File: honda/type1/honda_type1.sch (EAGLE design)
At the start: 3 parts, among them J1 501645-2620, J2 501645-3620

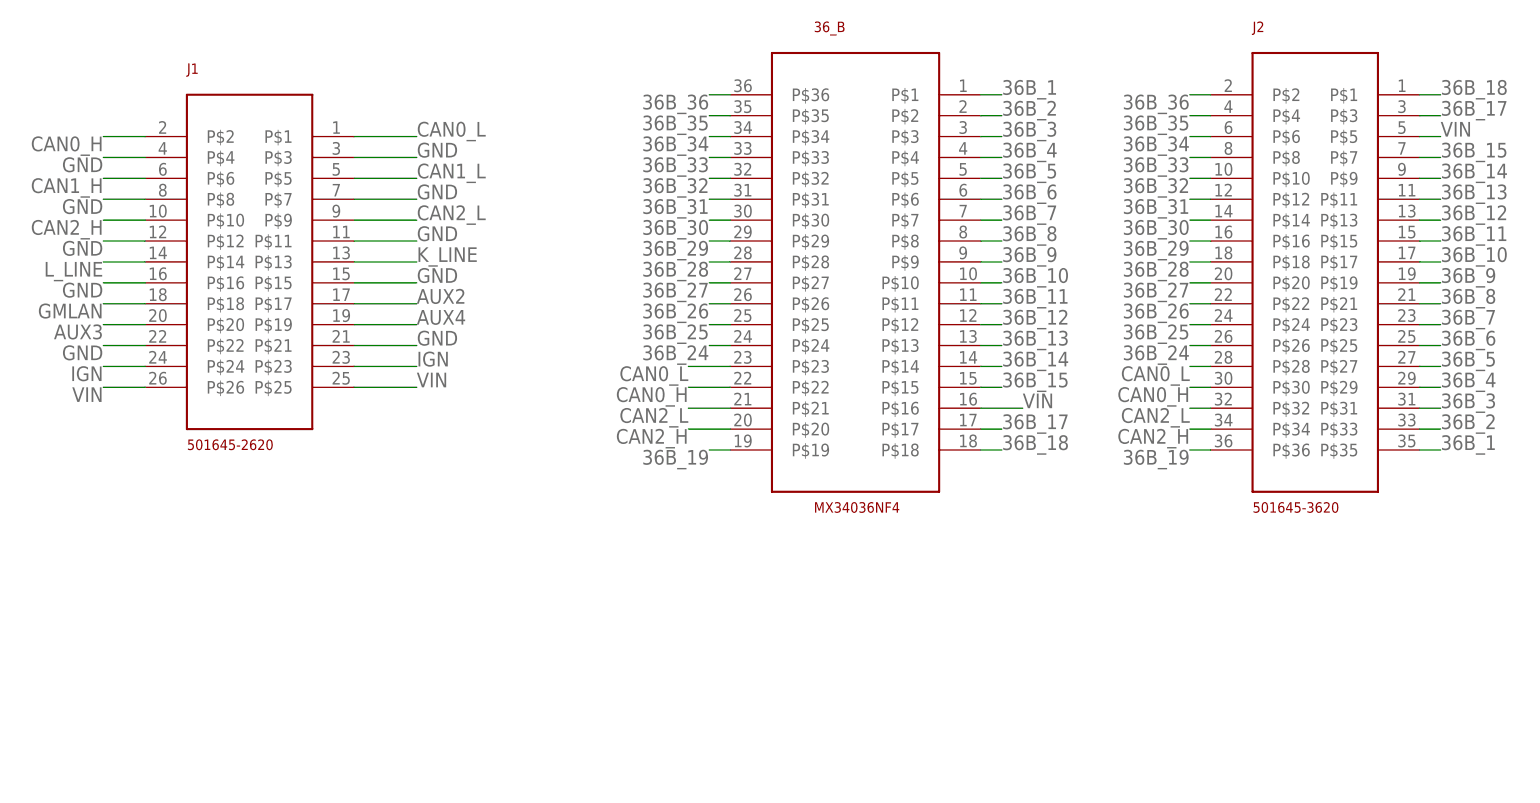
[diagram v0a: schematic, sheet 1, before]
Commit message: switch to rj45 for the interconnect
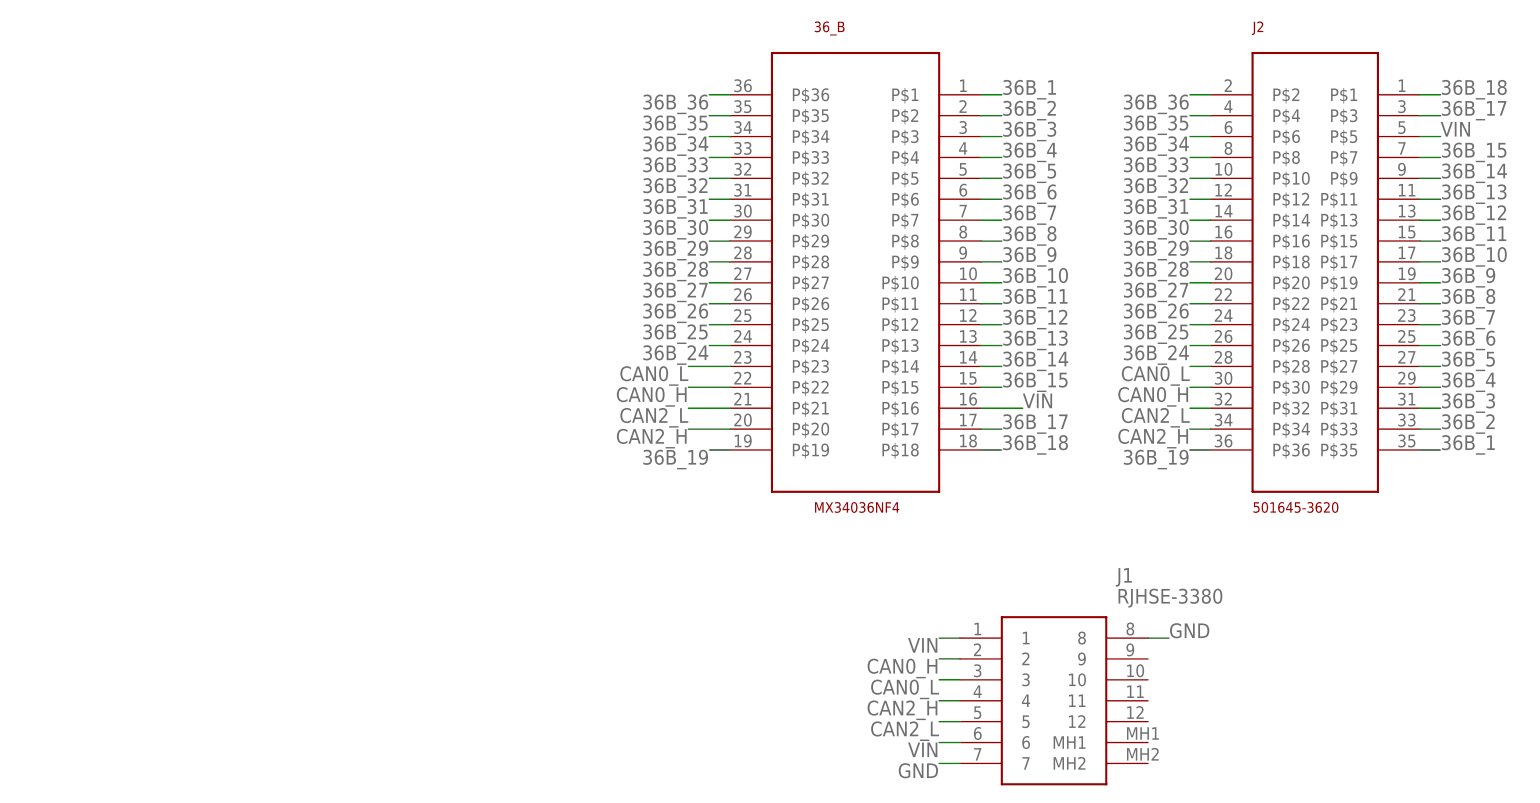
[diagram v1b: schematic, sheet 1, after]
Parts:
- J1: value 501645-2620 -> RJHSE-3380; device Souers:501645-2620 -> RJHSE-3380:RJHSE-3380
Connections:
- removed net AUX2: J1.P$17
- removed net AUX3: J1.P$20
- removed net AUX4: J1.P$19
- removed net CAN1_H: J1.P$6
- removed net CAN1_L: J1.P$5
- removed net GMLAN: J1.P$18
- removed net IGN: J1.P$23, J1.P$24
- removed net K_LINE: J1.P$13
- removed net L_LINE: J1.P$14
- net CAN0_H: now also J1.2; no longer J1.P$2
- net CAN0_L: now also J1.3; no longer J1.P$1
- net CAN2_H: now also J1.4; no longer J1.P$10
- net CAN2_L: now also J1.5; no longer J1.P$9
- net GND: now also J1.7, J1.8; no longer J1.P$11, J1.P$12, J1.P$15, J1.P$16, J1.P$21, J1.P$22, J1.P$3, J1.P$4, J1.P$7, J1.P$8
- net VIN: now also J1.1, J1.6; no longer J1.P$25, J1.P$26
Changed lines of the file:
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@@
 <parts>
 <part name="36_B" library="Souers" deviceset="MX34036NF4" device=""/>
-<part name="J1" library="Souers" deviceset="501645-2620" device=""/>
 <part name="J2" library="Souers" deviceset="501645-3620" device=""/>
+<part name="J1" library="RJHSE-3380" deviceset="RJHSE-3380" device=""/>
 </parts>
 <sheets>
@@
 <instances>
 <instance part="36_B" gate="G$1" x="22.86" y="10.16"/>
-<instance part="J1" gate="G$1" x="-58.42" y="7.62"/>
 <instance part="J2" gate="G$1" x="71.12" y="12.7"/>
+<instance part="J1" gate="G$1" x="33.02" y="-35.56"/>
 </instances>
 <busses>
 </busses>
 <nets>
-<net name="GND" class="0">
-<segment>
-<pinref part="J1" gate="G$1" pin="P$3"/>
-<wire x1="-40.64" y1="22.86" x2="-33.02" y2="22.86" width="0.1524" layer="91"/>
-<label x="-33.02" y="22.86" size="1.778" layer="95"/>
-</segment>
-<segment>
-<pinref part="J1" gate="G$1" pin="P$4"/>
-<wire x1="-66.04" y1="22.86" x2="-71.12" y2="22.86" width="0.1524" layer="91"/>
-<label x="-71.12" y="22.86" size="1.778" layer="95" rot="R180"/>
-</segment>
-<segment>
-<pinref part="J1" gate="G$1" pin="P$8"/>
-<wire x1="-66.04" y1="17.78" x2="-71.12" y2="17.78" width="0.1524" layer="91"/>
-<label x="-71.12" y="17.78" size="1.778" layer="95" rot="R180"/>
-</segment>
-<segment>
-<pinref part="J1" gate="G$1" pin="P$7"/>
-<wire x1="-40.64" y1="17.78" x2="-33.02" y2="17.78" width="0.1524" layer="91"/>
-<label x="-33.02" y="17.78" size="1.778" layer="95"/>
-</segment>
-<segment>
-<pinref part="J1" gate="G$1" pin="P$11"/>
-<wire x1="-40.64" y1="12.7" x2="-33.02" y2="12.7" width="0.1524" layer="91"/>
-<label x="-33.02" y="12.7" size="1.778" layer="95"/>
-</segment>
-<segment>
-<pinref part="J1" gate="G$1" pin="P$12"/>
-<wire x1="-66.04" y1="12.7" x2="-71.12" y2="12.7" width="0.1524" layer="91"/>
-<label x="-71.12" y="12.7" size="1.778" layer="95" rot="R180"/>
-</segment>
-<segment>
-<pinref part="J1" gate="G$1" pin="P$21"/>
-<wire x1="-40.64" y1="0" x2="-33.02" y2="0" width="0.1524" layer="91"/>
-<label x="-33.02" y="0" size="1.778" layer="95"/>
-</segment>
-<segment>
-<pinref part="J1" gate="G$1" pin="P$22"/>
-<wire x1="-66.04" y1="0" x2="-71.12" y2="0" width="0.1524" layer="91"/>
-<label x="-71.12" y="0" size="1.778" layer="95" rot="R180"/>
-</segment>
-<segment>
-<pinref part="J1" gate="G$1" pin="P$16"/>
-<wire x1="-66.04" y1="7.62" x2="-71.12" y2="7.62" width="0.1524" layer="91"/>
-<label x="-71.12" y="7.62" size="1.778" layer="95" rot="R180"/>
-</segment>
-<segment>
-<pinref part="J1" gate="G$1" pin="P$15"/>
-<wire x1="-40.64" y1="7.62" x2="-33.02" y2="7.62" width="0.1524" layer="91"/>
-<label x="-33.02" y="7.62" size="1.778" layer="95"/>
-</segment>
-</net>
-<net name="K_LINE" class="0">
-<segment>
-<pinref part="J1" gate="G$1" pin="P$13"/>
-<wire x1="-40.64" y1="10.16" x2="-33.02" y2="10.16" width="0.1524" layer="91"/>
-<label x="-33.02" y="10.16" size="1.778" layer="95"/>
-</segment>
-</net>
 <net name="VIN" class="1">
 <segment>
@@
 </segment>
 <segment>
-<pinref part="J1" gate="G$1" pin="P$25"/>
-<wire x1="-40.64" y1="-5.08" x2="-33.02" y2="-5.08" width="0.1524" layer="91"/>
-<label x="-33.02" y="-5.08" size="1.778" layer="95"/>
-</segment>
-<segment>
-<pinref part="J1" gate="G$1" pin="P$26"/>
-<wire x1="-66.04" y1="-5.08" x2="-71.12" y2="-5.08" width="0.1524" layer="91"/>
-<label x="-71.12" y="-5.08" size="1.778" layer="95" rot="R180"/>
-</segment>
-<segment>
 <pinref part="J2" gate="G$1" pin="P$5"/>
 <wire x1="88.9" y1="25.4" x2="91.44" y2="25.4" width="0.1524" layer="91"/>
 <label x="91.44" y="25.4" size="1.778" layer="95"/>
 </segment>
+<segment>
+<pinref part="J1" gate="G$1" pin="1"/>
+<wire x1="33.02" y1="-35.56" x2="30.48" y2="-35.56" width="0.1524" layer="91"/>
+<label x="30.48" y="-35.56" size="1.778" layer="95" rot="R180"/>
+</segment>
+<segment>
+<pinref part="J1" gate="G$1" pin="6"/>
+<wire x1="33.02" y1="-48.26" x2="30.48" y2="-48.26" width="0.1524" layer="91"/>
+<label x="30.48" y="-48.26" size="1.778" layer="95" rot="R180"/>
+</segment>
 </net>
 <net name="CAN2_H" class="0">
@@
 </segment>
 <segment>
-<pinref part="J1" gate="G$1" pin="P$10"/>
-<wire x1="-66.04" y1="15.24" x2="-71.12" y2="15.24" width="0.1524" layer="91"/>
-<label x="-71.12" y="15.24" size="1.778" layer="95" rot="R180"/>
-</segment>
-<segment>
 <pinref part="J2" gate="G$1" pin="P$34"/>
 <wire x1="63.5" y1="-10.16" x2="60.96" y2="-10.16" width="0.1524" layer="91"/>
 <label x="60.96" y="-10.16" size="1.778" layer="95" rot="R180"/>
 </segment>
+<segment>
+<pinref part="J1" gate="G$1" pin="4"/>
+<wire x1="33.02" y1="-43.18" x2="30.48" y2="-43.18" width="0.1524" layer="91"/>
+<label x="30.48" y="-43.18" size="1.778" layer="95" rot="R180"/>
+</segment>
 </net>
 <net name="CAN2_L" class="0">
@@
 </segment>
 <segment>
-<pinref part="J1" gate="G$1" pin="P$9"/>
-<wire x1="-40.64" y1="15.24" x2="-33.02" y2="15.24" width="0.1524" layer="91"/>
-<label x="-33.02" y="15.24" size="1.778" layer="95"/>
-</segment>
-<segment>
 <pinref part="J2" gate="G$1" pin="P$32"/>
 <wire x1="63.5" y1="-7.62" x2="60.96" y2="-7.62" width="0.1524" layer="91"/>
 <label x="60.96" y="-7.62" size="1.778" layer="95" rot="R180"/>
 </segment>
+<segment>
+<pinref part="J1" gate="G$1" pin="5"/>
+<wire x1="33.02" y1="-45.72" x2="30.48" y2="-45.72" width="0.1524" layer="91"/>
+<label x="30.48" y="-45.72" size="1.778" layer="95" rot="R180"/>
+</segment>
 </net>
 <net name="CAN0_H" class="0">
@@
 </segment>
 <segment>
-<pinref part="J1" gate="G$1" pin="P$2"/>
-<wire x1="-66.04" y1="25.4" x2="-71.12" y2="25.4" width="0.1524" layer="91"/>
-<label x="-71.12" y="25.4" size="1.778" layer="95" rot="R180"/>
-</segment>
-<segment>
 <pinref part="J2" gate="G$1" pin="P$30"/>
 <wire x1="63.5" y1="-5.08" x2="60.96" y2="-5.08" width="0.1524" layer="91"/>
 <label x="60.96" y="-5.08" size="1.778" layer="95" rot="R180"/>
 </segment>
+<segment>
+<pinref part="J1" gate="G$1" pin="2"/>
+<wire x1="33.02" y1="-38.1" x2="30.48" y2="-38.1" width="0.1524" layer="91"/>
+<label x="30.48" y="-38.1" size="1.778" layer="95" rot="R180"/>
+</segment>
 </net>
 <net name="CAN0_L" class="0">
@@
 </segment>
 <segment>
-<pinref part="J1" gate="G$1" pin="P$1"/>
-<wire x1="-40.64" y1="25.4" x2="-33.02" y2="25.4" width="0.1524" layer="91"/>
-<label x="-33.02" y="25.4" size="1.778" layer="95"/>
-</segment>
-<segment>
 <pinref part="J2" gate="G$1" pin="P$28"/>
 <wire x1="63.5" y1="-2.54" x2="60.96" y2="-2.54" width="0.1524" layer="91"/>
 <label x="60.96" y="-2.54" size="1.778" layer="95" rot="R180"/>
 </segment>
-</net>
-<net name="L_LINE" class="0">
-<segment>
-<pinref part="J1" gate="G$1" pin="P$14"/>
-<wire x1="-66.04" y1="10.16" x2="-71.12" y2="10.16" width="0.1524" layer="91"/>
-<label x="-71.12" y="10.16" size="1.778" layer="95" rot="R180"/>
-</segment>
-</net>
-<net name="IGN" class="1">
-<segment>
-<pinref part="J1" gate="G$1" pin="P$23"/>
-<wire x1="-40.64" y1="-2.54" x2="-33.02" y2="-2.54" width="0.1524" layer="91"/>
-<label x="-33.02" y="-2.54" size="1.778" layer="95"/>
-</segment>
-<segment>
-<pinref part="J1" gate="G$1" pin="P$24"/>
-<wire x1="-66.04" y1="-2.54" x2="-71.12" y2="-2.54" width="0.1524" layer="91"/>
-<label x="-71.12" y="-2.54" size="1.778" layer="95" rot="R180"/>
-</segment>
-</net>
-<net name="CAN1_L" class="0">
-<segment>
-<pinref part="J1" gate="G$1" pin="P$5"/>
-<wire x1="-40.64" y1="20.32" x2="-33.02" y2="20.32" width="0.1524" layer="91"/>
-<label x="-33.02" y="20.32" size="1.778" layer="95"/>
-</segment>
-</net>
-<net name="CAN1_H" class="0">
-<segment>
-<pinref part="J1" gate="G$1" pin="P$6"/>
-<wire x1="-66.04" y1="20.32" x2="-71.12" y2="20.32" width="0.1524" layer="91"/>
-<label x="-71.12" y="20.32" size="1.778" layer="95" rot="R180"/>
-</segment>
-</net>
-<net name="AUX2" class="0">
-<segment>
-<pinref part="J1" gate="G$1" pin="P$17"/>
-<wire x1="-40.64" y1="5.08" x2="-33.02" y2="5.08" width="0.1524" layer="91"/>
-<label x="-33.02" y="5.08" size="1.778" layer="95"/>
-</segment>
-</net>
-<net name="AUX3" class="0">
-<segment>
-<pinref part="J1" gate="G$1" pin="P$20"/>
-<wire x1="-66.04" y1="2.54" x2="-71.12" y2="2.54" width="0.1524" layer="91"/>
-<label x="-71.12" y="2.54" size="1.778" layer="95" rot="R180"/>
-</segment>
-</net>
-<net name="AUX4" class="0">
-<segment>
-<pinref part="J1" gate="G$1" pin="P$19"/>
-<wire x1="-40.64" y1="2.54" x2="-33.02" y2="2.54" width="0.1524" layer="91"/>
-<label x="-33.02" y="2.54" size="1.778" layer="95"/>
-</segment>
-</net>
-<net name="GMLAN" class="0">
-<segment>
-<pinref part="J1" gate="G$1" pin="P$18"/>
-<wire x1="-66.04" y1="5.08" x2="-71.12" y2="5.08" width="0.1524" layer="91"/>
-<label x="-71.12" y="5.08" size="1.778" layer="95" rot="R180"/>
+<segment>
+<pinref part="J1" gate="G$1" pin="3"/>
+<wire x1="33.02" y1="-40.64" x2="30.48" y2="-40.64" width="0.1524" layer="91"/>
+<label x="30.48" y="-40.64" size="1.778" layer="95" rot="R180"/>
 </segment>
 </net>
@@
 </segment>
 </net>
+<net name="GND" class="1">
+<segment>
+<pinref part="J1" gate="G$1" pin="8"/>
+<wire x1="55.88" y1="-35.56" x2="58.42" y2="-35.56" width="0.1524" layer="91"/>
+<label x="58.42" y="-35.56" size="1.778" layer="95"/>
+</segment>
+<segment>
+<pinref part="J1" gate="G$1" pin="7"/>
+<wire x1="33.02" y1="-50.8" x2="30.48" y2="-50.8" width="0.1524" layer="91"/>
+<label x="30.48" y="-50.8" size="1.778" layer="95" rot="R180"/>
+</segment>
+</net>

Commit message: push
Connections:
- removed net CAN0_H: 36_B.P$22, J1.2, J2.P$30
- removed net CAN0_L: 36_B.P$23, J1.3, J2.P$28
- new net CAN1_H: 36_B.P$20, J1.4, J2.P$34
- new net CAN1_L: 36_B.P$21, J1.5, J2.P$32
- net CAN2_H: now also 36_B.P$22, J1.2, J2.P$30; no longer 36_B.P$20, J1.4, J2.P$34
- net CAN2_L: now also 36_B.P$23, J1.3, J2.P$28; no longer 36_B.P$21, J1.5, J2.P$32
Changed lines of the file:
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@@
 </segment>
 </net>
-<net name="CAN2_H" class="0">
+<net name="CAN1_H" class="0">
 <segment>
 <pinref part="36_B" gate="G$1" pin="P$20"/>
@@
 </segment>
 </net>
-<net name="CAN2_L" class="0">
+<net name="CAN1_L" class="0">
 <segment>
 <pinref part="36_B" gate="G$1" pin="P$21"/>
@@
 </segment>
 </net>
-<net name="CAN0_H" class="0">
+<net name="CAN2_H" class="0">
 <segment>
 <pinref part="36_B" gate="G$1" pin="P$22"/>
@@
 </segment>
 </net>
-<net name="CAN0_L" class="0">
+<net name="CAN2_L" class="0">
 <segment>
 <pinref part="36_B" gate="G$1" pin="P$23"/>
